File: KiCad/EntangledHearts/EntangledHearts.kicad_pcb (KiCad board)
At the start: 2 copper layers, 91.4 x 30.5 mm, 65 parts

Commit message: CHG: rewiring of front pcb
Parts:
- BatteryConnector1: moved to F.Cu
- moved C_NP1 164.4 mm to (63.5, 44.5)
- moved D1 164.3 mm to (63.5, 44.5)
- moved D2 158.5 mm to (81.2, 53.3), turned to 120 degrees
- moved C_NP2 158.4 mm to (81.3, 53.3), turned to 120 degrees
- moved C_NP6 158.3 mm to (45.7, 53.3), turned to -120 degrees
- moved D6 158.3 mm to (45.7, 53.3), turned to -120 degrees
- moved Display1 152.9 mm to (67.3, 52.1)
- moved C_NP3 148.3 mm to (81.3, 73.7), turned to 60 degrees
- moved D3 148.3 mm to (81.3, 73.7), turned to 60 degrees
- moved C_NP5 148.0 mm to (45.7, 73.7), turned to -60 degrees
- moved D5 148.0 mm to (45.7, 73.7), turned to -60 degrees
- moved D4 141.7 mm to (63.5, 82.5)
- moved C_NP4 141.6 mm to (63.5, 82.5)
- moved GND2 103.9 mm to (110.5, 41.9)
- moved MPU1 103.9 mm to (118.1, 55.9)
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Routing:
- net VCC_Top: track 159.5 -> 0.00 mm, vias 8 -> 0
- net GND_Top: track 164.2 -> 69.3 mm, vias 6 -> 0
- net GND: track 196.0 -> 207.4 mm
- net Net-(D1-DOUT): track 22.1 -> 16.4 mm
- net SCL_Top: track 22.8 -> 17.2 mm
- net Net-(D4-DOUT): track 21.6 -> 16.5 mm
- net SDA_Top: track 18.5 -> 13.4 mm
- net Net-(D1-DIN): track 4.31 -> 0.00 mm, vias 1 -> 0
- net Net-(D5-DOUT): track 21.3 -> 17.3 mm
- net Net-(BM1-V_{BAT}): track 33.5 -> 36.7 mm, vias 3 -> 2
- net Net-(D3-DOUT): track 19.2 -> 17.3 mm
- net Net-(D2-DOUT): track 18.5 -> 17.2 mm
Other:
- board size 91.4 x 30.5 mm -> 199.4 x 68.6 mm

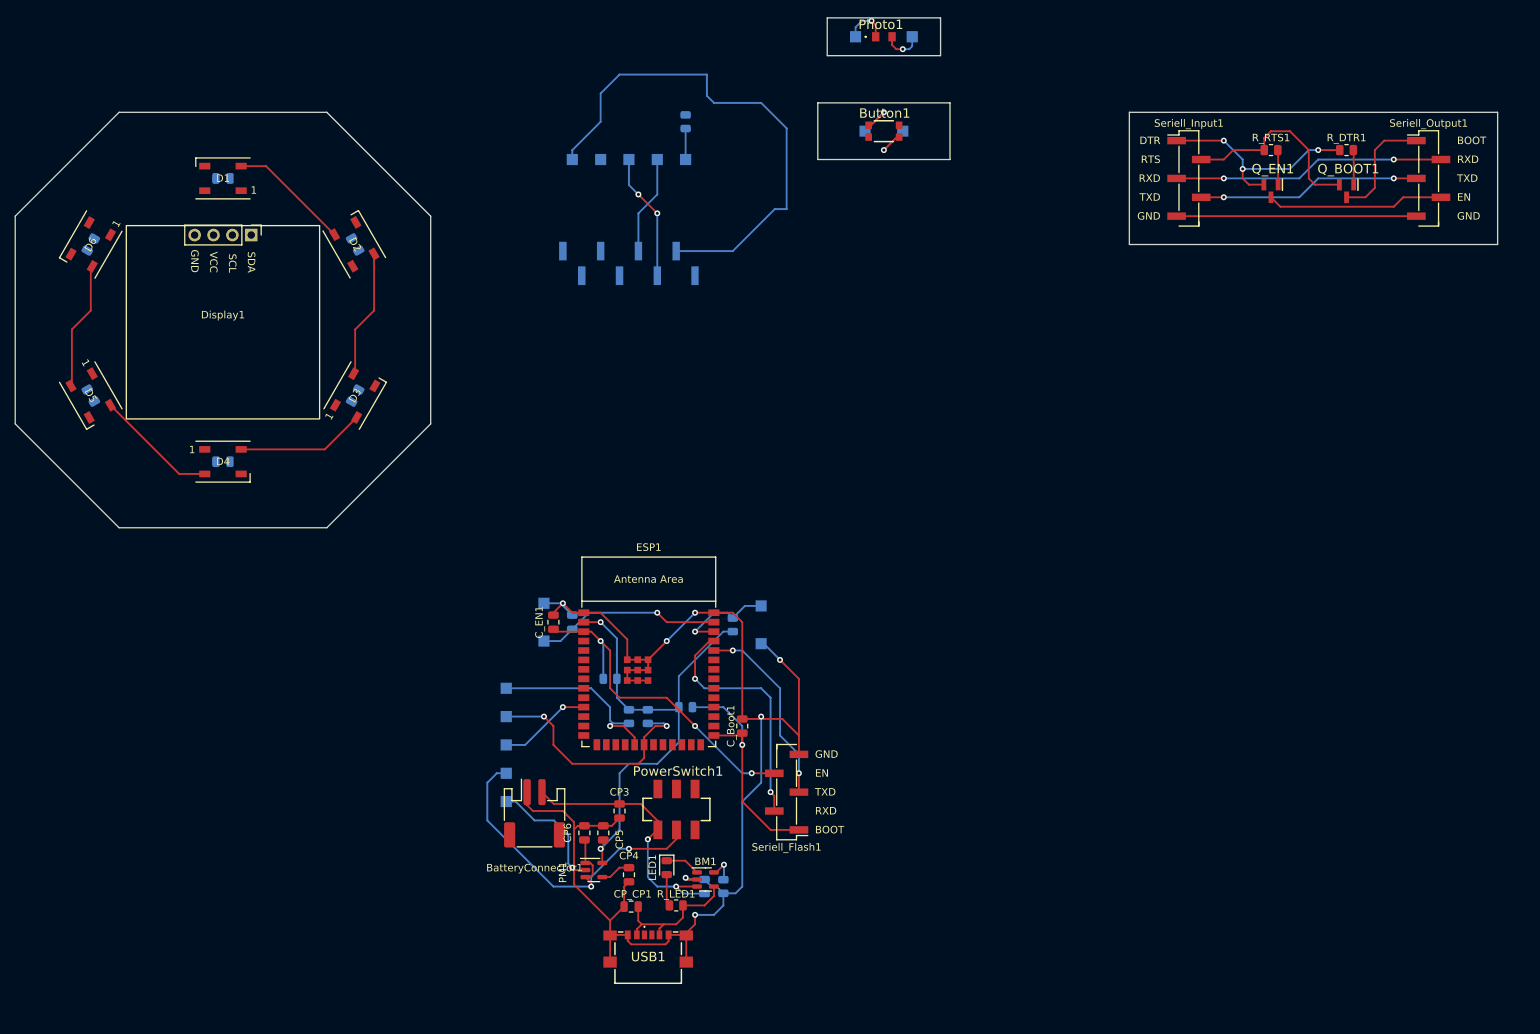
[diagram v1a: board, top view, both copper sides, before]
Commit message: ADD: all components on front PCB placed
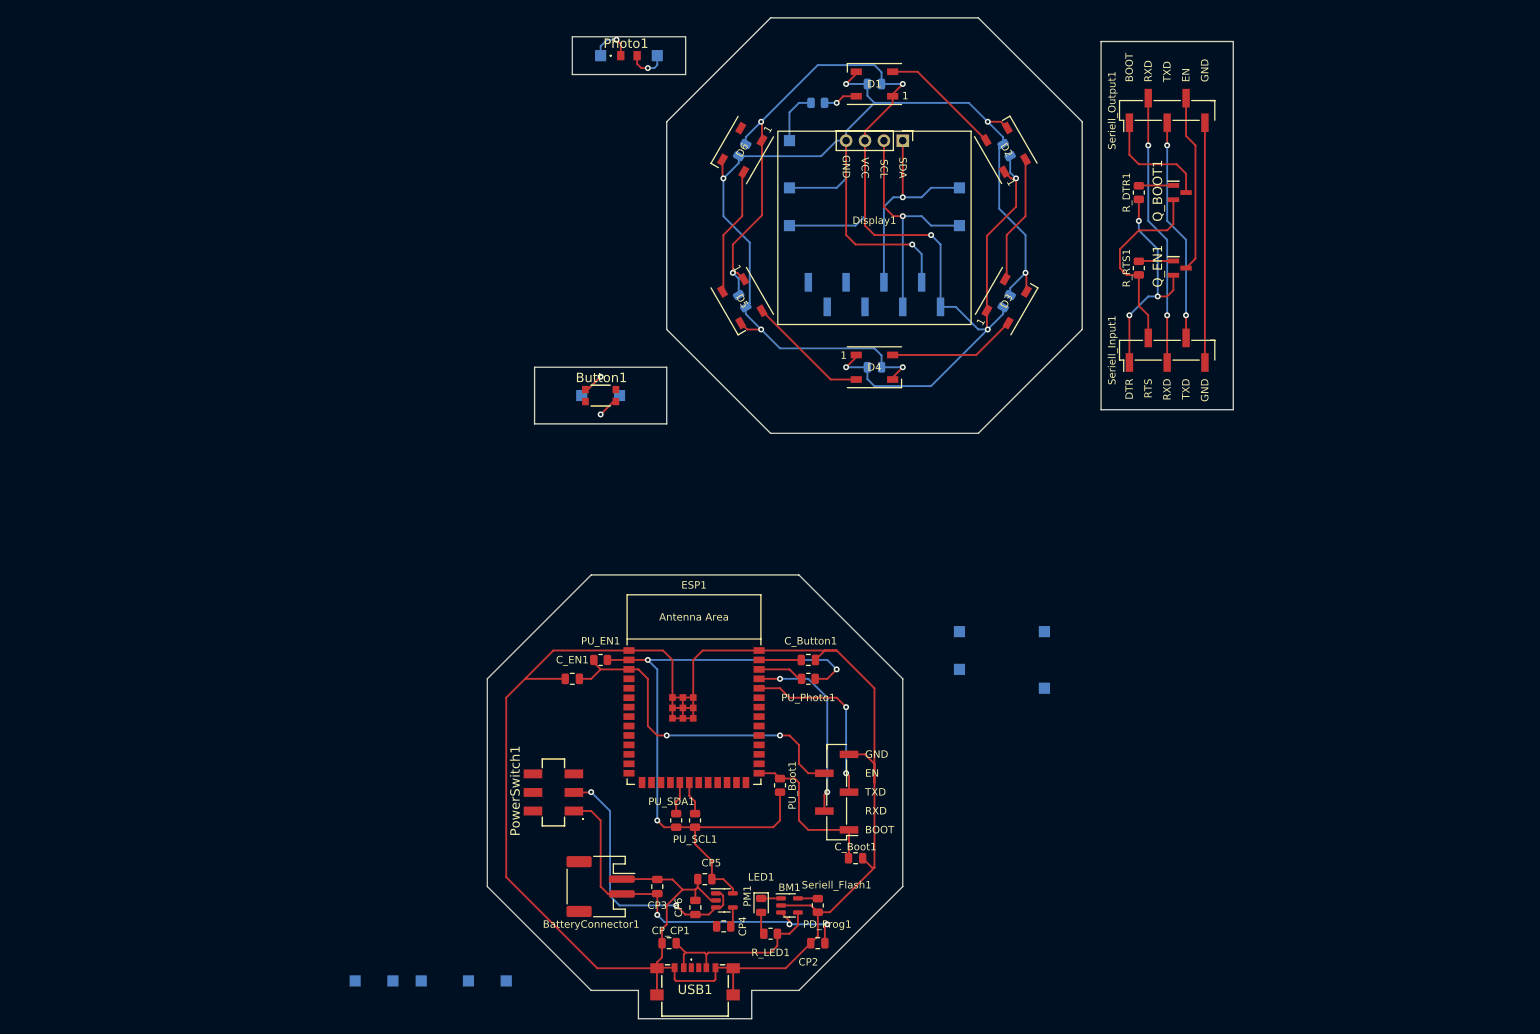
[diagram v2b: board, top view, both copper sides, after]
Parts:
- CP2, C_Button1, PD_Prog1, PU_Boot1, PU_EN1, PU_Photo1, PU_SCL1, PU_SDA1: moved to F.Cu
- moved C_NP1 88.5 mm to (151.1, 31.8)
- moved C_NP2 88.5 mm to (168.9, 40.6)
- moved C_NP3 88.5 mm to (168.9, 61.0)
- moved C_NP4 88.5 mm to (151.1, 69.8)
- moved C_NP5 88.5 mm to (133.3, 61.0)
- moved C_NP6 88.5 mm to (133.3, 40.6)
- moved D1 88.5 mm to (151.1, 31.8)
- moved D3 88.5 mm to (168.9, 61.0)
- moved D4 88.5 mm to (151.1, 69.8)
- moved D5 88.5 mm to (133.3, 61.0)
- moved D6 88.5 mm to (133.3, 40.6)
- moved Display1 88.5 mm to (154.9, 39.4)
- moved D2 88.5 mm to (168.8, 40.6)
- moved ButtonA1 56.0 mm to (162.6, 110.5)
- moved ButtonB1 56.0 mm to (162.6, 105.4)
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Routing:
- net VCC_Top: track 0.00 -> 181.9 mm, vias 0 -> 7
- net GND_Top: track 69.3 -> 176.1 mm, vias 0 -> 7
- net GND: track 207.4 -> 251.7 mm, vias 8 -> 0
- net SCL_Bottom: track 32.1 -> 4.51 mm, vias 2 -> 0
- net +3.3V: track 65.7 -> 89.9 mm, vias 2 -> 3
- net SDA_Bottom: track 25.0 -> 4.39 mm, vias 1 -> 0
- net Button: track 25.0 -> 5.68 mm, vias 1 -> 0
- net SDA_Top: track 13.4 -> 29.0 mm, vias 0 -> 1
- net Net-(BM1-V_{BAT}): track 36.7 -> 52.1 mm, vias 2 -> 3
- net SCL_Top: track 17.2 -> 32.3 mm, vias 2 -> 1
- net +4V: track 50.1 -> 36.5 mm
- net NeoPixel_Bottom: track 12.5 -> 0.00 mm, vias 1 -> 0
- net Boot: track 32.7 -> 22.1 mm, vias 1 -> 0
- net RXD: track 33.1 -> 25.6 mm
- net Photo: track 13.4 -> 6.24 mm, vias 1 -> 0
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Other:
- board size 199.4 x 68.6 mm -> 100.3 x 134.6 mm

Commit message: ADD: all components connected
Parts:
- moved ButtonB1 59.1 mm to (104.1, 114.3)
- moved ButtonA1 58.9 mm to (104.1, 118.1), turned to 90 degrees
- moved NeoPixel1 46.0 mm to (123.2, 133.3)
- moved SDA1 41.5 mm to (127.0, 133.3)
- moved SCL1 39.2 mm to (130.8, 133.3)
- moved VCC1 38.1 mm to (134.6, 133.3)
- moved GND1 38.1 mm to (119.4, 133.3)
- moved C_Button1 33.9 mm to (109.2, 116.8), turned to 90 degrees
- moved PhotoA1 25.7 mm to (149.9, 114.3)
- moved PhotoB1 24.7 mm to (149.9, 118.1)
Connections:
- ESP1 pad 39: Button -> unconnected-(ESP1-GPIO1/TOUCH1/ADC1_CH0-Pad39)
- ESP1 pad 6: unconnected-(ESP1-GPIO6/TOUCH6/ADC1_CH5-Pad6) -> Button
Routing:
- net GND: track 251.7 -> 277.1 mm, vias 0 -> 3
- net +4V: track 36.5 -> 54.9 mm
- net NeoPixel_Bottom: track 0.00 -> 15.5 mm, vias 0 -> 1
- net Button: track 5.68 -> 15.5 mm, vias 0 -> 1
- net Photo: track 6.24 -> 15.8 mm, vias 0 -> 1
- net SCL_Bottom: track 4.51 -> 12.7 mm, vias 0 -> 1
- net SDA_Bottom: track 4.39 -> 10.5 mm, vias 0 -> 1
- net +3.3V: track 89.9 -> 85.2 mm

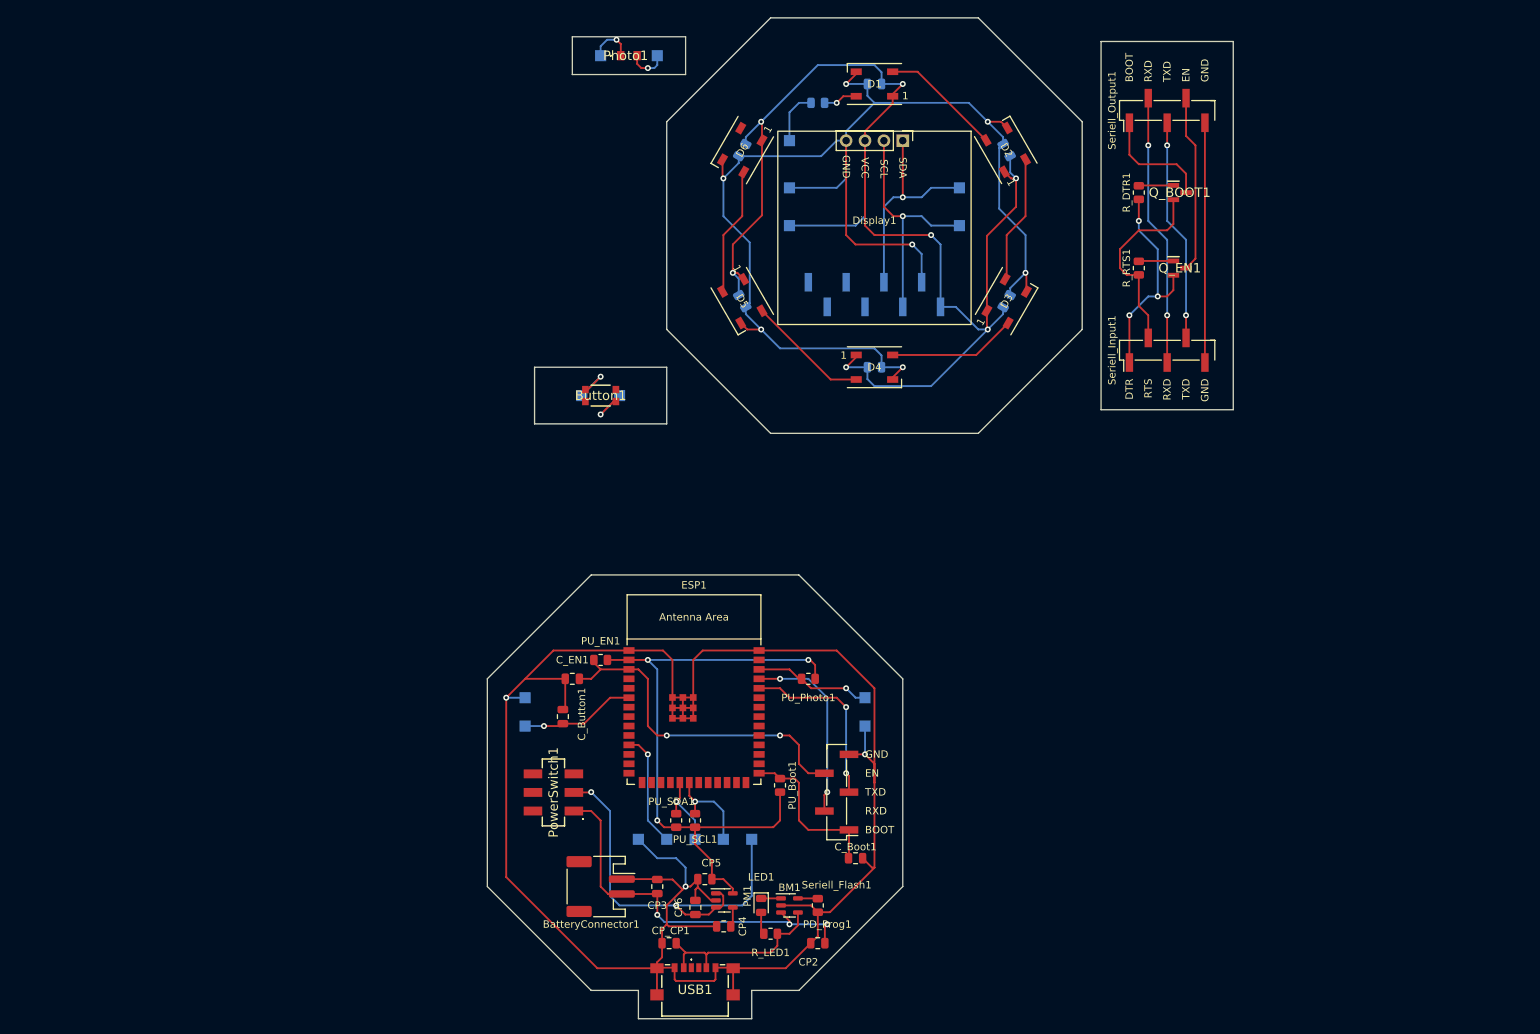
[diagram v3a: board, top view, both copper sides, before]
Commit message: CHG: Alignment changed
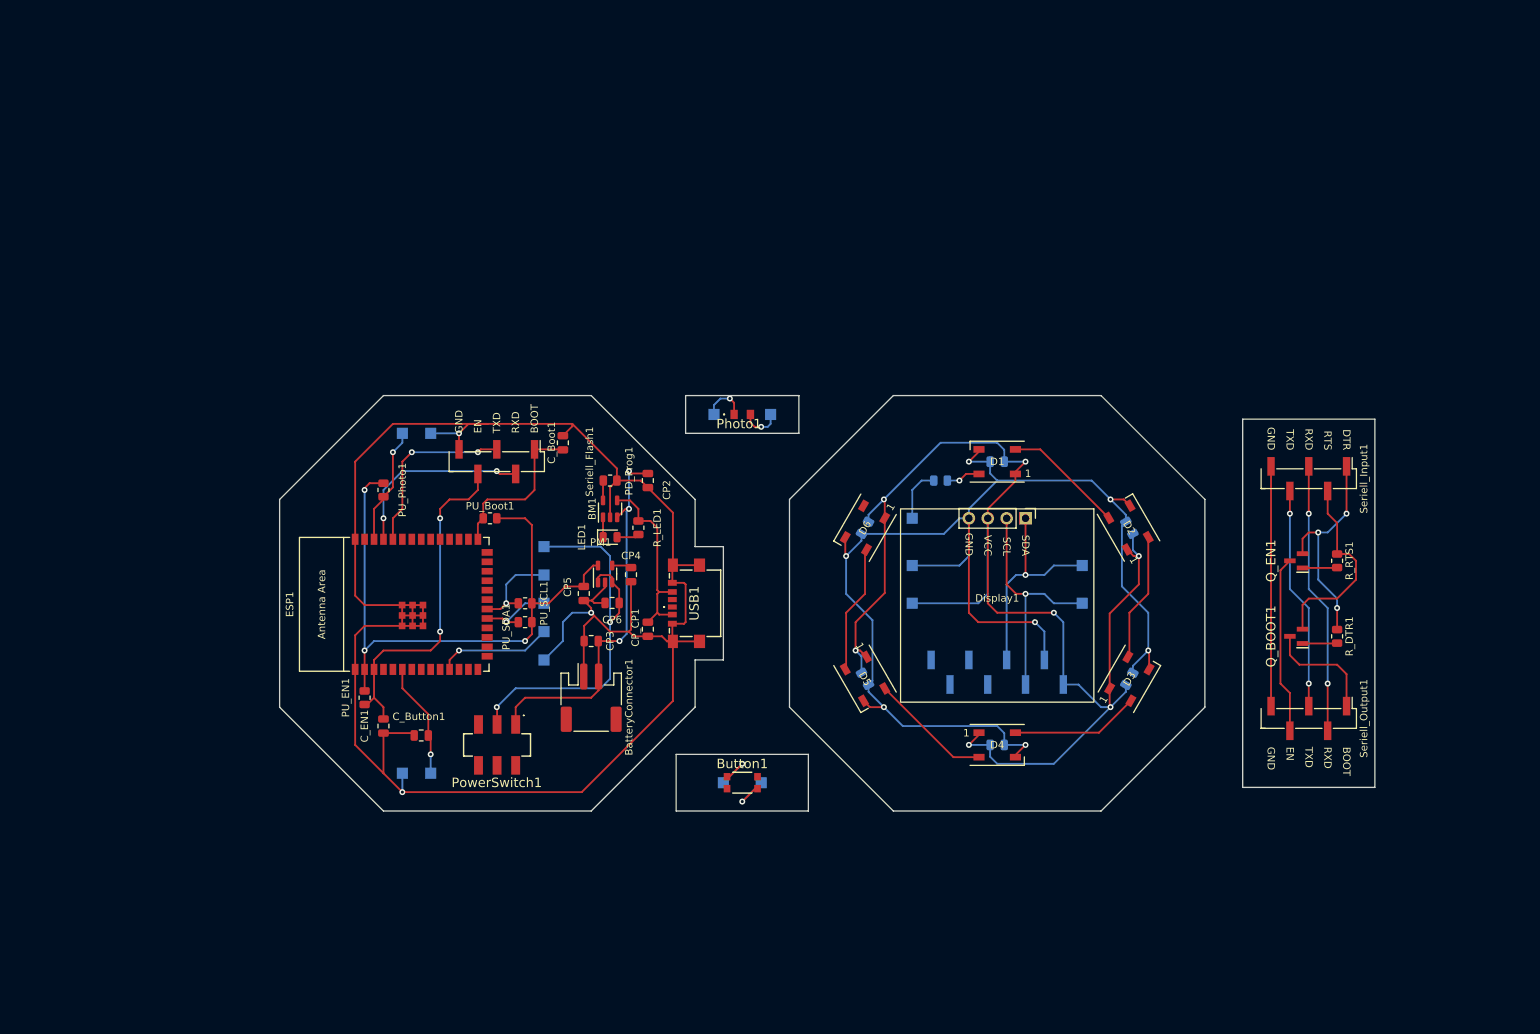
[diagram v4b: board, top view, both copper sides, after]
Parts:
- moved Seriell_Output1 84.0 mm to (209.6, 117.1), turned to -90 degrees
- moved PhotoA1 71.7 mm to (87.6, 78.7), turned to -90 degrees
- moved PhotoB1 70.4 mm to (91.4, 78.7), turned to -90 degrees
- moved C_Boot1 68.4 mm to (109.2, 80.0), turned to -90 degrees
- moved CP2 66.3 mm to (120.7, 85.1), turned to -90 degrees
- moved R_DTR1 65.4 mm to (213.4, 106.0), turned to -90 degrees
- moved Seriell_Flash1 63.8 mm to (100.3, 82.5), turned to -90 degrees
- moved PD_Prog1 63.6 mm to (115.6, 85.1), turned to 0 degrees
- moved PU_Photo1 62.5 mm to (85.1, 86.4), turned to 90 degrees
- moved Q_BOOT1 61.7 mm to (207.9, 106.0), turned to 180 degrees
- moved BM1 58.5 mm to (115.6, 88.9), turned to 90 degrees
- moved R_LED1 57.4 mm to (119.4, 91.4), turned to -90 degrees
- moved Button1 55.4 mm to (133.3, 125.7)
- moved ButtonA2 55.4 mm to (130.8, 125.7)
- moved ButtonB2 55.4 mm to (135.9, 125.7)
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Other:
- board size 100.3 x 134.6 mm -> 147.3 x 55.9 mm
